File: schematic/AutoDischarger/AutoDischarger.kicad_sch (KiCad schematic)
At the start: 10 parts, among them IC1 AP7375-50SA-7, IC2 PIC18F15Q40-I_SS, J1 ICSP, J2 Balance Lead

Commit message: Initial pcb layout
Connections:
- net Discharge Control/C1: now also IC2.6 (RC4); no longer IC2.16 (RC0)
- net Discharge Control/C2: now also IC2.7 (RC3); no longer IC2.15 (RC1)
- net Discharge Control/C3: now also IC2.5 (RC5); no longer IC2.14 (RC2)
- net Discharge Control/C4: now also IC2.15 (RC1); no longer IC2.7 (RC3)
- net Discharge Control/C5: now also IC2.14 (RC2); no longer IC2.6 (RC4)
- net Discharge Control/C6: now also IC2.16 (RC0); no longer IC2.5 (RC5)
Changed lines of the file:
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@@
-    (stroke (width 0) (type default) (color 0 0 0 0))
-  )
-  (wire (pts (xy 170.815 68.58) (xy 170.815 128.27))
-    (stroke (width 0) (type default) (color 0 0 0 0))
-  )
-  (wire (pts (xy 173.99 130.175) (xy 118.745 130.175))
     (stroke (width 0) (type default) (color 0 0 0 0))
   )
@@
     (stroke (width 0) (type default) (color 0 0 0 0))
   )
-  (wire (pts (xy 122.555 125.73) (xy 167.005 125.73))
+  (wire (pts (xy 124.46 107.315) (xy 124.46 125.73))
     (stroke (width 0) (type default) (color 0 0 0 0))
   )
@@
     (stroke (width 0) (type default) (color 0 0 0 0))
   )
-  (wire (pts (xy 91.44 71.12) (xy 111.76 71.12))
-    (stroke (width 0) (type default) (color 0 0 0 0))
-  )
   (wire (pts (xy 17.145 50.8) (xy 24.765 50.8))
     (stroke (width 0) (type default) (color 0 0 0 0))
@@
     (stroke (width 0) (type default) (color 0 0 0 0))
   )
+  (wire (pts (xy 91.44 110.49) (xy 126.365 110.49))
+    (stroke (width 0) (type default) (color 0 0 0 0))
+  )
   (wire (pts (xy 208.28 63.5) (xy 211.455 63.5))
     (stroke (width 0) (type default) (color 0 0 0 0))
@@
     (stroke (width 0) (type default) (color 0 0 0 0))
   )
-  (wire (pts (xy 118.745 110.49) (xy 126.365 110.49))
+  (wire (pts (xy 170.815 71.12) (xy 170.815 128.27))
     (stroke (width 0) (type default) (color 0 0 0 0))
   )
@@
     (stroke (width 0) (type default) (color 0 0 0 0))
   )
+  (wire (pts (xy 160.02 71.12) (xy 170.815 71.12))
+    (stroke (width 0) (type default) (color 0 0 0 0))
+  )
   (wire (pts (xy 115.57 90.805) (xy 164.465 90.805))
     (stroke (width 0) (type default) (color 0 0 0 0))
   )
-  (wire (pts (xy 160.02 71.12) (xy 173.99 71.12))
+  (wire (pts (xy 74.93 113.665) (xy 126.365 113.665))
     (stroke (width 0) (type default) (color 0 0 0 0))
   )
@@
     (stroke (width 0) (type default) (color 0 0 0 0))
   )
+  (wire (pts (xy 71.755 68.58) (xy 111.76 68.58))
+    (stroke (width 0) (type default) (color 0 0 0 0))
+  )
   (wire (pts (xy 160.655 78.74) (xy 160.655 83.185))
     (stroke (width 0) (type default) (color 0 0 0 0))
@@
     (stroke (width 0) (type default) (color 0 0 0 0))
   )
+  (wire (pts (xy 167.005 68.58) (xy 160.02 68.58))
+    (stroke (width 0) (type default) (color 0 0 0 0))
+  )
   (wire (pts (xy 151.765 150.495) (xy 184.785 150.495))
     (stroke (width 0) (type default) (color 0 0 0 0))
   )
-  (wire (pts (xy 167.005 66.04) (xy 160.02 66.04))
-    (stroke (width 0) (type default) (color 0 0 0 0))
-  )
-  (wire (pts (xy 170.815 68.58) (xy 160.02 68.58))
-    (stroke (width 0) (type default) (color 0 0 0 0))
-  )
   (wire (pts (xy 151.765 153.67) (xy 187.325 153.67))
     (stroke (width 0) (type default) (color 0 0 0 0))
@@
     (stroke (width 0) (type default) (color 0 0 0 0))
   )
+  (wire (pts (xy 126.365 104.14) (xy 121.92 104.14))
+    (stroke (width 0) (type default) (color 0 0 0 0))
+  )
   (wire (pts (xy 81.28 76.2) (xy 111.76 76.2))
     (stroke (width 0) (type default) (color 0 0 0 0))
@@
     (stroke (width 0) (type default) (color 0 0 0 0))
   )
-  (wire (pts (xy 126.365 116.84) (xy 122.555 116.84))
-    (stroke (width 0) (type default) (color 0 0 0 0))
-  )
   (wire (pts (xy 64.77 33.655) (xy 64.77 50.8))
     (stroke (width 0) (type default) (color 0 0 0 0))
   )
-  (wire (pts (xy 170.815 128.27) (xy 120.65 128.27))
+  (wire (pts (xy 118.745 100.965) (xy 118.745 130.175))
     (stroke (width 0) (type default) (color 0 0 0 0))
   )
@@
     (stroke (width 0) (type default) (color 0 0 0 0))
   )
+  (wire (pts (xy 118.745 130.175) (xy 173.99 130.175))
+    (stroke (width 0) (type default) (color 0 0 0 0))
+  )
   (wire (pts (xy 160.02 55.88) (xy 167.005 55.88))
     (stroke (width 0) (type default) (color 0 0 0 0))
@@
     (stroke (width 0) (type default) (color 0 0 0 0))
   )
+  (wire (pts (xy 91.44 66.04) (xy 111.76 66.04))
+    (stroke (width 0) (type default) (color 0 0 0 0))
+  )
   (wire (pts (xy 151.765 156.845) (xy 189.865 156.845))
     (stroke (width 0) (type default) (color 0 0 0 0))
@@
     (stroke (width 0) (type default) (color 0 0 0 0))
   )
+  (wire (pts (xy 71.755 116.84) (xy 126.365 116.84))
+    (stroke (width 0) (type default) (color 0 0 0 0))
+  )
   (wire (pts (xy 95.25 168.91) (xy 161.29 168.91))
     (stroke (width 0) (type default) (color 0 0 0 0))
@@
     (stroke (width 0) (type default) (color 0 0 0 0))
   )
-  (wire (pts (xy 74.93 104.14) (xy 74.93 68.58))
-    (stroke (width 0) (type default) (color 0 0 0 0))
-  )
   (wire (pts (xy 29.21 92.71) (xy 60.325 92.71))
     (stroke (width 0) (type default) (color 0 0 0 0))
   )
-  (wire (pts (xy 120.65 113.665) (xy 126.365 113.665))
-    (stroke (width 0) (type default) (color 0 0 0 0))
-  )
   (wire (pts (xy 95.25 58.42) (xy 111.76 58.42))
     (stroke (width 0) (type default) (color 0 0 0 0))
@@
     (stroke (width 0) (type default) (color 0 0 0 0))
   )
-  (wire (pts (xy 120.65 128.27) (xy 120.65 113.665))
-    (stroke (width 0) (type default) (color 0 0 0 0))
-  )
   (wire (pts (xy 126.365 156.845) (xy 98.425 156.845))
     (stroke (width 0) (type default) (color 0 0 0 0))
@@
     (stroke (width 0) (type default) (color 0 0 0 0))
   )
+  (wire (pts (xy 160.02 66.04) (xy 173.99 66.04))
+    (stroke (width 0) (type default) (color 0 0 0 0))
+  )
+  (wire (pts (xy 121.92 104.14) (xy 121.92 128.27))
+    (stroke (width 0) (type default) (color 0 0 0 0))
+  )
   (wire (pts (xy 187.325 130.175) (xy 187.325 153.67))
     (stroke (width 0) (type default) (color 0 0 0 0))
@@
     (stroke (width 0) (type default) (color 0 0 0 0))
   )
-  (wire (pts (xy 91.44 107.315) (xy 91.44 71.12))
+  (wire (pts (xy 91.44 66.04) (xy 91.44 110.49))
     (stroke (width 0) (type default) (color 0 0 0 0))
   )
@@
     (stroke (width 0) (type default) (color 0 0 0 0))
   )
-  (wire (pts (xy 173.99 71.12) (xy 173.99 130.175))
+  (wire (pts (xy 173.99 66.04) (xy 173.99 130.175))
     (stroke (width 0) (type default) (color 0 0 0 0))
   )
@@
     (stroke (width 0) (type default) (color 0 0 0 0))
   )
-  (wire (pts (xy 122.555 116.84) (xy 122.555 125.73))
-    (stroke (width 0) (type default) (color 0 0 0 0))
-  )
   (wire (pts (xy 107.95 63.5) (xy 111.76 63.5))
     (stroke (width 0) (type default) (color 0 0 0 0))
   )
-  (wire (pts (xy 126.365 100.965) (xy 71.755 100.965))
-    (stroke (width 0) (type default) (color 0 0 0 0))
-  )
-  (wire (pts (xy 126.365 107.315) (xy 91.44 107.315))
-    (stroke (width 0) (type default) (color 0 0 0 0))
-  )
-  (wire (pts (xy 74.93 68.58) (xy 111.76 68.58))
-    (stroke (width 0) (type default) (color 0 0 0 0))
-  )
   (wire (pts (xy 192.405 135.255) (xy 194.31 135.255))
     (stroke (width 0) (type default) (color 0 0 0 0))
   )
+  (wire (pts (xy 121.92 128.27) (xy 170.815 128.27))
+    (stroke (width 0) (type default) (color 0 0 0 0))
+  )
   (wire (pts (xy 161.29 160.02) (xy 192.405 160.02))
     (stroke (width 0) (type default) (color 0 0 0 0))
   )
+  (wire (pts (xy 74.93 71.12) (xy 74.93 113.665))
+    (stroke (width 0) (type default) (color 0 0 0 0))
+  )
   (wire (pts (xy 126.365 147.32) (xy 111.76 147.32))
     (stroke (width 0) (type default) (color 0 0 0 0))
@@
     (stroke (width 0) (type default) (color 0 0 0 0))
   )
+  (wire (pts (xy 124.46 125.73) (xy 167.005 125.73))
+    (stroke (width 0) (type default) (color 0 0 0 0))
+  )
   (wire (pts (xy 200.025 130.175) (xy 187.325 130.175))
     (stroke (width 0) (type default) (color 0 0 0 0))
@@
     (stroke (width 0) (type default) (color 0 0 0 0))
   )
-  (wire (pts (xy 126.365 104.14) (xy 74.93 104.14))
-    (stroke (width 0) (type default) (color 0 0 0 0))
-  )
   (wire (pts (xy 111.76 147.32) (xy 111.76 86.995))
     (stroke (width 0) (type default) (color 0 0 0 0))
@@
     (stroke (width 0) (type default) (color 0 0 0 0))
   )
-  (wire (pts (xy 71.755 100.965) (xy 71.755 66.04))
+  (wire (pts (xy 126.365 100.965) (xy 118.745 100.965))
     (stroke (width 0) (type default) (color 0 0 0 0))
   )
@@
     (stroke (width 0) (type default) (color 0 0 0 0))
   )
+  (wire (pts (xy 111.76 71.12) (xy 74.93 71.12))
+    (stroke (width 0) (type default) (color 0 0 0 0))
+  )
   (wire (pts (xy 179.705 122.555) (xy 209.55 122.555))
     (stroke (width 0) (type default) (color 0 0 0 0))
   )
-  (wire (pts (xy 167.005 125.73) (xy 167.005 66.04))
-    (stroke (width 0) (type default) (color 0 0 0 0))
-  )
-  (wire (pts (xy 118.745 130.175) (xy 118.745 110.49))
+  (wire (pts (xy 126.365 107.315) (xy 124.46 107.315))
+    (stroke (width 0) (type default) (color 0 0 0 0))
+  )
+  (wire (pts (xy 167.005 68.58) (xy 167.005 125.73))
     (stroke (width 0) (type default) (color 0 0 0 0))
   )
@@
     (stroke (width 0) (type default) (color 0 0 0 0))
   )
-  (wire (pts (xy 71.755 66.04) (xy 111.76 66.04))
-    (stroke (width 0) (type default) (color 0 0 0 0))
-  )
   (wire (pts (xy 60.325 103.505) (xy 60.325 105.41))
     (stroke (width 0) (type default) (color 0 0 0 0))
@@
     (stroke (width 0) (type default) (color 0 0 0 0))
   )
+  (wire (pts (xy 71.755 68.58) (xy 71.755 116.84))
+    (stroke (width 0) (type default) (color 0 0 0 0))
+  )

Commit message: Changed 5V regulator
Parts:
- removed IC1: AP7375-50SA-7, Package_TO_SOT_SMD:SOT-23, symbol SamacSys_Parts:MCP1703AT-5002E_CB
- added IC1: AP7375-50W5-7, SOT95P285X140-5N, symbol SamacSys_Parts2:AP7375-50W5-7
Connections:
- net +5V: now also IC1.5 (VOUT)
- net +8V: now also IC1.1 (VIN), IC1.3 (EN)
- net GND: now also IC1.2 (GND), IC1.4 (NC)

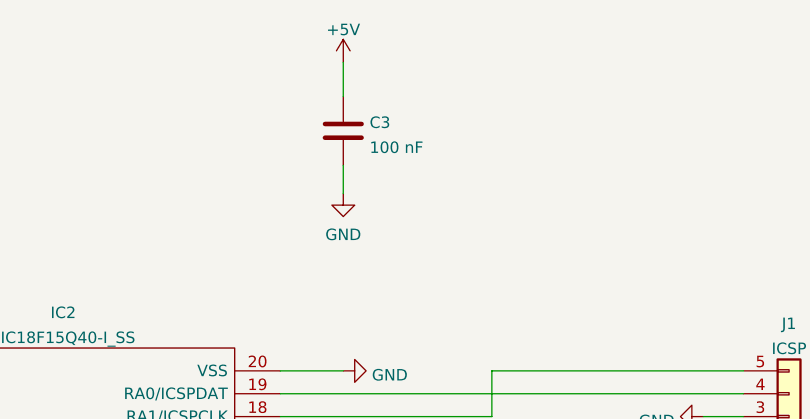
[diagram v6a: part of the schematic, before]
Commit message: Updated BOM and fixed some labels
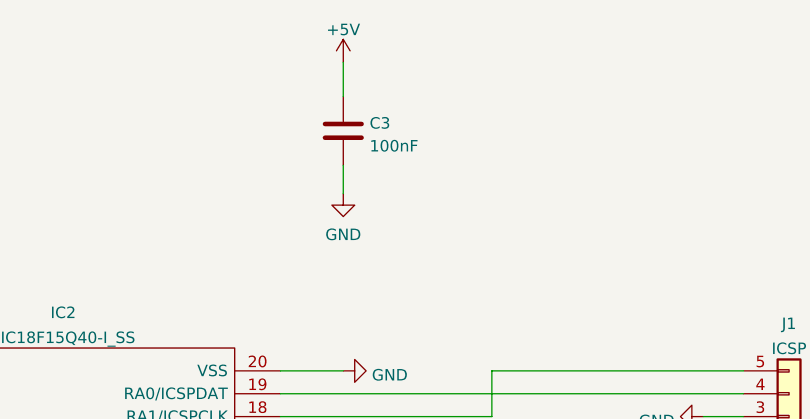
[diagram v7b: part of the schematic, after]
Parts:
- C3: value 100 nF -> 100nF
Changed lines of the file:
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@@
   (title_block
     (title "Lipo Auto Discharger/Balancer")
-    (date "2022-11-06")
+    (date "2023-01-25")
     (rev "1.0")
     (company "Quantum Embedded Systems")
@@
   (symbol (lib_id "Device:C") (at 167.005 29.21 0) (unit 1)
     (in_bom yes) (on_board yes) (fields_autoplaced)
-    (property "Reference" "C3" (id 0) (at 169.926 28.3015 0)
-      (effects (font (size 1.27 1.27)) (justify left))
-    )
-    (property "Value" "100 nF" (id 1) (at 169.926 31.0766 0)
+    (property "Reference" "C3" (id 0) (at 169.926 28.3753 0)
+      (effects (font (size 1.27 1.27)) (justify left))
+    )
+    (property "Value" "100nF" (id 1) (at 169.926 30.9122 0)
       (effects (font (size 1.27 1.27)) (justify left))
     )
@@
     )
     (path "/c84e2900-b7ec-460d-a445-a7a49231dc91"
-      (reference "C3") (unit 1) (value "100 nF") (footprint "Capacitor_SMD:C_0603_1608Metric")
+      (reference "C3") (unit 1) (value "100nF") (footprint "Capacitor_SMD:C_0603_1608Metric")
     )
     (path "/7294720e-84fa-44e2-8e91-1fa25a9bb61d/4c49df8c-374e-4085-8ec3-1251865adf1a"

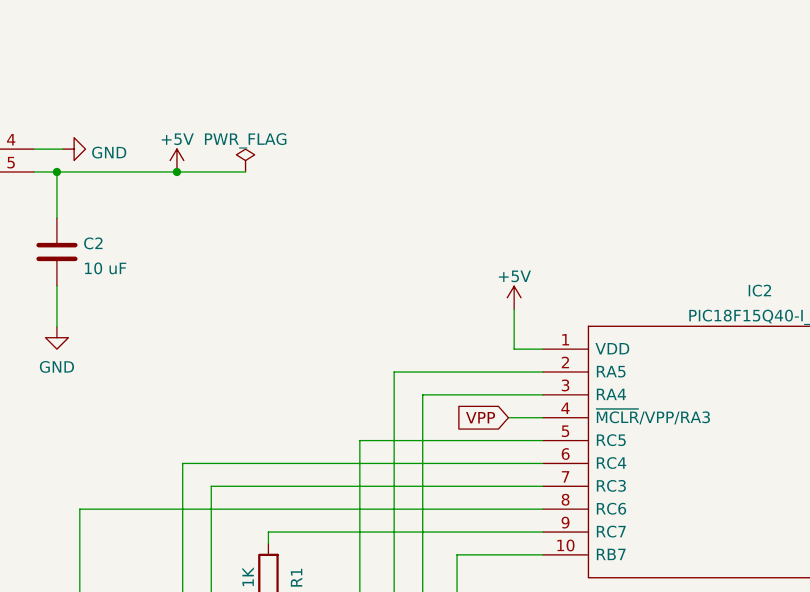
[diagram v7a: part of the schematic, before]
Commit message: Added pullup to MCLR
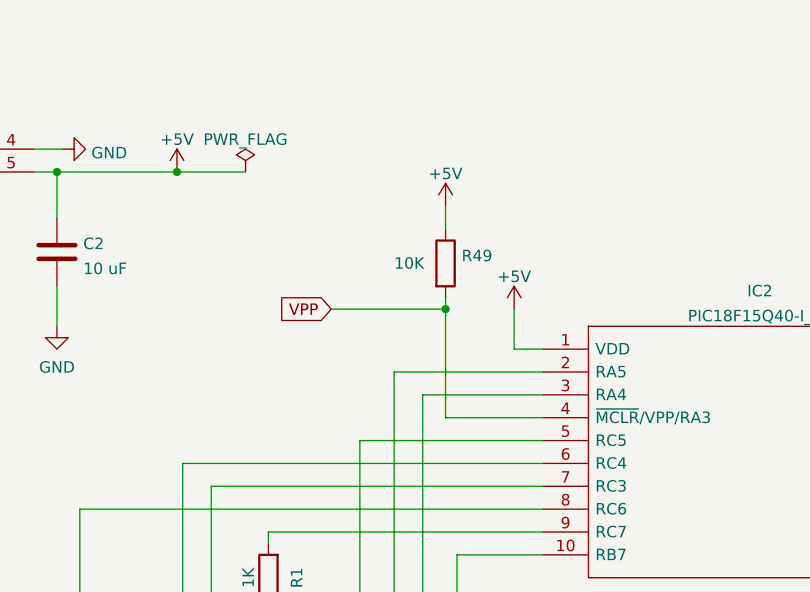
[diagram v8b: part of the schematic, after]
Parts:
- added R49: 10K, Resistor_SMD:R_0603_1608Metric, symbol Device:R
- IC1: footprint SOT95P285X140-5N -> SamacSys_Parts:SOT95P285X140-5N
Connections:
- net +5V: now also R49.1
- net VPP: now also R49.2
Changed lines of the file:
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@@
   (junction (at 24.765 33.655) (diameter 0) (color 0 0 0 0)
   )
+  (junction (at 100.965 51.435) (diameter 0) (color 0 0 0 0)
+  )
   (junction (at 57.785 36.195) (diameter 0) (color 0 0 0 0)
   )
@@
     (stroke (width 0) (type default) (color 0 0 0 0))
   )
+  (wire (pts (xy 111.76 63.5) (xy 100.965 63.5))
+    (stroke (width 0) (type default) (color 0 0 0 0))
+  )
   (wire (pts (xy 91.44 110.49) (xy 126.365 110.49))
     (stroke (width 0) (type default) (color 0 0 0 0))
@@
     (stroke (width 0) (type default) (color 0 0 0 0))
   )
+  (wire (pts (xy 88.265 51.435) (xy 100.965 51.435))
+    (stroke (width 0) (type default) (color 0 0 0 0))
+  )
   (wire (pts (xy 24.765 33.655) (xy 27.305 33.655))
     (stroke (width 0) (type default) (color 0 0 0 0))
@@
     (stroke (width 0) (type default) (color 0 0 0 0))
   )
+  (wire (pts (xy 100.965 63.5) (xy 100.965 51.435))
+    (stroke (width 0) (type default) (color 0 0 0 0))
+  )
   (wire (pts (xy 160.02 66.04) (xy 173.99 66.04))
     (stroke (width 0) (type default) (color 0 0 0 0))
@@
     (stroke (width 0) (type default) (color 0 0 0 0))
   )
-  (wire (pts (xy 107.95 63.5) (xy 111.76 63.5))
-    (stroke (width 0) (type default) (color 0 0 0 0))
-  )
   (wire (pts (xy 192.405 135.255) (xy 194.31 135.255))
     (stroke (width 0) (type default) (color 0 0 0 0))
@@
     (stroke (width 0) (type default) (color 0 0 0 0))
   )
+  (wire (pts (xy 100.965 51.435) (xy 100.965 50.165))
+    (stroke (width 0) (type default) (color 0 0 0 0))
+  )
   (wire (pts (xy 201.93 156.845) (xy 201.93 154.94))
     (stroke (width 0) (type default) (color 0 0 0 0))
@@
   )
   (wire (pts (xy 167.005 68.58) (xy 167.005 125.73))
+    (stroke (width 0) (type default) (color 0 0 0 0))
+  )
+  (wire (pts (xy 100.965 40.005) (xy 100.965 42.545))
     (stroke (width 0) (type default) (color 0 0 0 0))
   )
@@
     )
   )
-  (global_label "VPP" (shape input) (at 107.95 63.5 180) (fields_autoplaced)
+  (global_label "VPP" (shape input) (at 88.265 51.435 180) (fields_autoplaced)
     (effects (font (size 1.27 1.27)) (justify right))
-    (property "Intersheet References" "${INTERSHEET_REFS}" (id 0) (at 101.9083 63.4206 0)
+    (property "Intersheet References" "${INTERSHEET_REFS}" (id 0) (at 82.2233 51.3556 0)
       (effects (font (size 1.27 1.27)) (justify right) hide)
     )
@@
     (pin "2")
   )
+  (symbol (lib_id "power:+5V") (at 100.965 40.005 0) (unit 1)
+    (in_bom yes) (on_board yes) (fields_autoplaced)
+    (property "Reference" "#PWR0104" (id 0) (at 100.965 43.815 0)
+      (effects (font (size 1.27 1.27)) hide)
+    )
+    (property "Value" "+5V" (id 1) (at 100.965 36.4005 0))
+    (property "Footprint" "" (id 2) (at 100.965 40.005 0)
+      (effects (font (size 1.27 1.27)) hide)
+    )
+    (property "Datasheet" "" (id 3) (at 100.965 40.005 0)
+      (effects (font (size 1.27 1.27)) hide)
+    )
+    (pin "1")
+  )
   (symbol (lib_id "power:GND") (at 24.765 53.34 0) (unit 1)
     (in_bom yes) (on_board yes) (fields_autoplaced)
@@
     (property "Reference" "IC1" (id 0) (at 41.275 27.466 0))
     (property "Value" "AP7375-50W5-7" (id 1) (at 41.275 30.0029 0))
-    (property "Footprint" "SOT95P285X140-5N" (id 2) (at 51.435 31.115 0)
+    (property "Footprint" "SamacSys_Parts:SOT95P285X140-5N" (id 2) (at 51.435 31.115 0)
       (effects (font (size 1.27 1.27)) (justify left) hide)
     )
@@
     (pin "1")
   )
+  (symbol (lib_id "Device:R") (at 100.965 46.355 0) (unit 1)
+    (in_bom yes) (on_board yes)
+    (property "Reference" "R49" (id 0) (at 102.743 45.5203 0)
+      (effects (font (size 1.27 1.27)) (justify left))
+    )
+    (property "Value" "10K" (id 1) (at 95.25 46.355 0)
+      (effects (font (size 1.27 1.27)) (justify left))
+    )
+    (property "Footprint" "Resistor_SMD:R_0603_1608Metric" (id 2) (at 99.187 46.355 90)
+      (effects (font (size 1.27 1.27)) hide)
+    )
+    (property "Datasheet" "~" (id 3) (at 100.965 46.355 0)
+      (effects (font (size 1.27 1.27)) hide)
+    )
+    (pin "1")
+    (pin "2")
+  )
   (symbol (lib_id "power:GND") (at 29.845 105.41 0) (unit 1)
     (in_bom yes) (on_board yes) (fields_autoplaced)
@@
       (reference "#PWR0103") (unit 1) (value "+8V") (footprint "")
     )
+    (path "/49081f32-9003-4389-8815-19f1a70ee6be"
+      (reference "#PWR0104") (unit 1) (value "+5V") (footprint "")
+    )
     (path "/cd8226e0-a6bc-45cd-9c50-e74e92e2c36b"
       (reference "C1") (unit 1) (value "1 uF") (footprint "Capacitor_SMD:C_0603_1608Metric")
@@
     )
     (path "/9600303c-eba1-457e-9f70-13ecef000f46"
-      (reference "IC1") (unit 1) (value "AP7375-50W5-7") (footprint "SOT95P285X140-5N")
+      (reference "IC1") (unit 1) (value "AP7375-50W5-7") (footprint "SamacSys_Parts:SOT95P285X140-5N")
     )
     (path "/b96fe6ac-3535-4455-ab88-ed77f5e46d6e"
@@
       (reference "R48") (unit 1) (value "120R") (footprint "Resistor_SMD:R_1206_3216Metric")
     )
+    (path "/f548fbd4-145f-4199-a993-e251b83854ab"
+      (reference "R49") (unit 1) (value "10K") (footprint "Resistor_SMD:R_0603_1608Metric")
+    )
     (path "/d542974b-bf56-489e-a6b8-1e42bddea5f7"
